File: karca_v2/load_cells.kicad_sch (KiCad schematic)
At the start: 16 parts, among them J4 LoadCell_1_2, J5 LoadCell_3_4, U2 NUP4202, U3 MCP3208, U4 NUP4202, U5 NUP4202, U6 TLV9304xD, U7 TLV9304xD

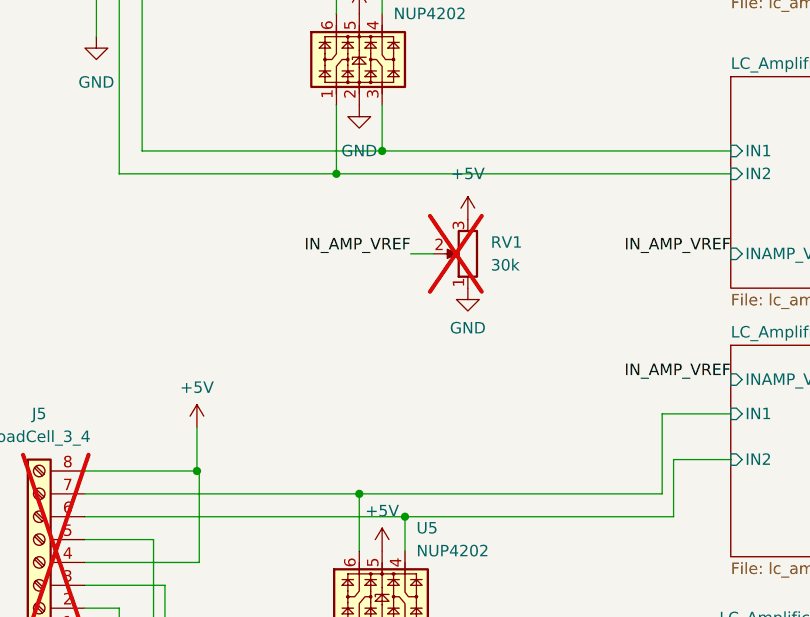
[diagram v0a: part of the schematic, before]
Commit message: reorganized ADCs
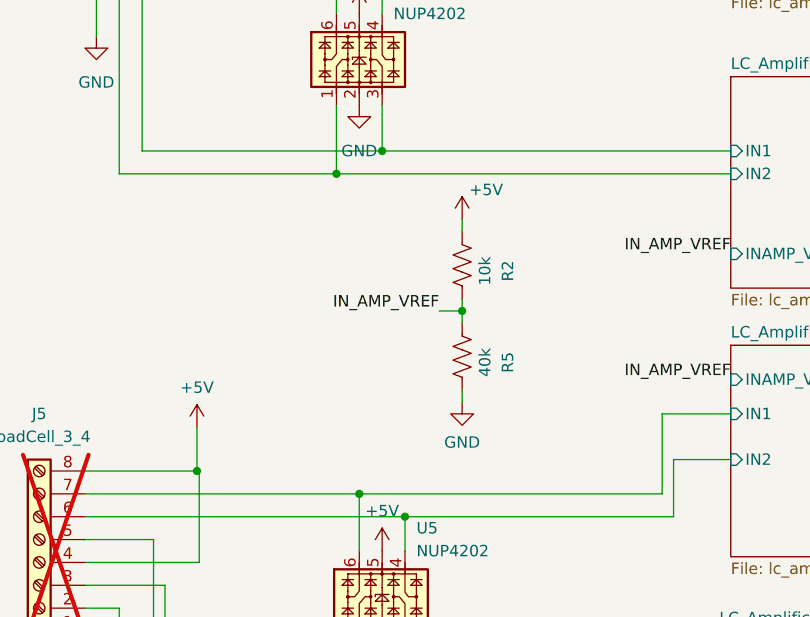
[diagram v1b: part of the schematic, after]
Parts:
- removed RV1: 30k, Potentiometer_THT:Potentiometer_Bourns_3296W_Vertical, symbol Device:R_Potentiometer
- added R2: 10k, Resistor_SMD:R_1206_3216Metric, symbol Device:R_US
- added R5: 40k, Resistor_SMD:R_1206_3216Metric, symbol Device:R_US
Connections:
- net +5V: now also R2.1
- net GND: now also R5.2
- net IN_AMP_VREF: now also R2.2, R5.1
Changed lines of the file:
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@@
 	(title_block
 		(title "kARCA 2.0 Engine Control System")
-		(date "2024-12-16")
-		(rev "1.1")
+		(date "2026-03-23")
+		(rev "1.2")
 		(company "Rice Eclipse")
 		(comment 1 "Designed by Deepak Narayan")
@@
 	)
 	(junction
+		(at 104.14 87.63)
+		(diameter 0)
+		(color 0 0 0 0)
+	)
+	(junction
 		(at 213.995 104.14)
 		(diameter 0)
@@
 	(wire
 		(pts
-			(xy 100.965 81.28) (xy 98.425 81.28)
+			(xy 104.14 87.63) (xy 101.6 87.63)
 		)
 		(stroke
@@
 	(wire
 		(pts
+			(xy 104.14 96.52) (xy 104.14 97.79)
+		)
+		(stroke
+			(width 0)
+			(type default)
+		)
+	)
+	(wire
+		(pts
 			(xy 133.985 104.14) (xy 127.635 104.14)
 		)
@@
 	(wire
 		(pts
+			(xy 104.14 87.63) (xy 104.14 88.9)
+		)
+		(stroke
+			(width 0)
+			(type default)
+		)
+	)
+	(wire
+		(pts
 			(xy 213.995 104.14) (xy 216.281 104.14)
 		)
@@
 	(wire
 		(pts
+			(xy 104.14 86.36) (xy 104.14 87.63)
+		)
+		(stroke
+			(width 0)
+			(type default)
+		)
+	)
+	(wire
+		(pts
 			(xy 95.25 154.94) (xy 95.25 151.13)
 		)
@@
 	(wire
 		(pts
+			(xy 104.14 77.47) (xy 104.14 78.74)
+		)
+		(stroke
+			(width 0)
+			(type default)
+		)
+	)
+	(wire
+		(pts
 			(xy 92.71 124.46) (xy 92.71 132.08)
 		)
@@
 	)
 	(label "IN_AMP_VREF"
-		(at 98.425 81.28 180)
+		(at 101.6 87.63 180)
 		(effects
 			(font
@@
 	)
 	(symbol
-		(lib_id "Device:R_Potentiometer")
-		(at 104.775 81.28 180)
+		(lib_id "Device:R_US")
+		(at 104.14 92.71 0)
 		(unit 1)
 		(exclude_from_sim no)
-		(in_bom no)
+		(in_bom yes)
 		(on_board yes)
-		(dnp yes)
-		(fields_autoplaced yes)
-		(property "Reference" "RV1"
-			(at 107.315 80.01 0)
+		(dnp no)
+		(property "Reference" "R5"
+			(at 109.22 93.345 90)
 			(effects
 				(font
 					(size 1.27 1.27)
 				)
-				(justify right)
 			)
 		)
-		(property "Value" "30k"
-			(at 107.315 82.55 0)
+		(property "Value" "40k"
+			(at 106.68 93.345 90)
 			(effects
 				(font
 					(size 1.27 1.27)
 				)
-				(justify right)
 			)
 		)
-		(property "Footprint" "Potentiometer_THT:Potentiometer_Bourns_3296W_Vertical"
-			(at 104.775 81.28 0)
+		(property "Footprint" "Resistor_SMD:R_1206_3216Metric"
+			(at 105.156 92.964 90)
 			(effects
 				(font
@@
 		)
 		(property "Datasheet" "~"
-			(at 104.775 81.28 0)
+			(at 104.14 92.71 0)
 			(effects
 				(font
@@
 		)
 		(property "Description" ""
-			(at 104.775 81.28 0)
+			(at 104.14 92.71 0)
 			(effects
 				(font
@@
 			)
 		)
-		(pin "3"
+		(pin "1"
+		)
+		(pin "2"
+		)
+		(instances
+			(project "karca_v2"
+				(path "/29cf4797-56f2-4f57-ae95-7df639362e3c/ddbef897-b93d-4056-8606-b8e89931524a"
+					(reference "R5")
+					(unit 1)
+				)
+			)
+		)
+	)
+	(symbol
+		(lib_id "Device:R_US")
+		(at 104.14 82.55 0)
+		(unit 1)
+		(exclude_from_sim no)
+		(in_bom yes)
+		(on_board yes)
+		(dnp no)
+		(property "Reference" "R2"
+			(at 109.22 83.185 90)
+			(effects
+				(font
+					(size 1.27 1.27)
+				)
+			)
+		)
+		(property "Value" "10k"
+			(at 106.68 83.185 90)
+			(effects
+				(font
+					(size 1.27 1.27)
+				)
+			)
+		)
+		(property "Footprint" "Resistor_SMD:R_1206_3216Metric"
+			(at 105.156 82.804 90)
+			(effects
+				(font
+					(size 1.27 1.27)
+				)
+				(hide yes)
+			)
+		)
+		(property "Datasheet" "~"
+			(at 104.14 82.55 0)
+			(effects
+				(font
+					(size 1.27 1.27)
+				)
+				(hide yes)
+			)
+		)
+		(property "Description" ""
+			(at 104.14 82.55 0)
+			(effects
+				(font
+					(size 1.27 1.27)
+				)
+				(hide yes)
+			)
 		)
 		(pin "1"
@@
 			(project "karca_v2"
 				(path "/29cf4797-56f2-4f57-ae95-7df639362e3c/ddbef897-b93d-4056-8606-b8e89931524a"
-					(reference "RV1")
+					(reference "R2")
 					(unit 1)
 				)
@@
 	(symbol
 		(lib_id "power:+5V")
-		(at 104.775 77.47 0)
+		(at 104.14 77.47 0)
 		(unit 1)
 		(exclude_from_sim no)
@@
 		(on_board yes)
 		(dnp no)
-		(fields_autoplaced yes)
 		(property "Reference" "#PWR021"
-			(at 104.775 81.28 0)
+			(at 104.14 81.28 0)
 			(effects
 				(font
@@
 		)
 		(property "Value" "+5V"
-			(at 104.775 72.39 0)
+			(at 106.807 74.168 0)
 			(effects
 				(font
@@
 		)
 		(property "Footprint" ""
-			(at 104.775 77.47 0)
+			(at 104.14 77.47 0)
 			(effects
 				(font
@@
 		)
 		(property "Datasheet" ""
-			(at 104.775 77.47 0)
+			(at 104.14 77.47 0)
 			(effects
 				(font
@@
 		)
 		(property "Description" ""
-			(at 104.775 77.47 0)
+			(at 104.14 77.47 0)
 			(effects
 				(font
@@
 	(symbol
 		(lib_id "power:GND")
-		(at 104.775 85.09 0)
+		(at 104.14 97.79 0)
 		(mirror y)
 		(unit 1)
@@
 		(fields_autoplaced yes)
 		(property "Reference" "#PWR023"
-			(at 104.775 91.44 0)
+			(at 104.14 104.14 0)
 			(effects
 				(font
@@
 		)
 		(property "Value" "GND"
-			(at 104.775 89.535 0)
+			(at 104.14 102.235 0)
 			(effects
 				(font
@@
 		)
 		(property "Footprint" ""
-			(at 104.775 85.09 0)
+			(at 104.14 97.79 0)
 			(effects
 				(font
@@
 		)
 		(property "Datasheet" ""
-			(at 104.775 85.09 0)
+			(at 104.14 97.79 0)
 			(effects
 				(font
@@
 		)
 		(property "Description" ""
-			(at 104.775 85.09 0)
+			(at 104.14 97.79 0)
 			(effects
 				(font

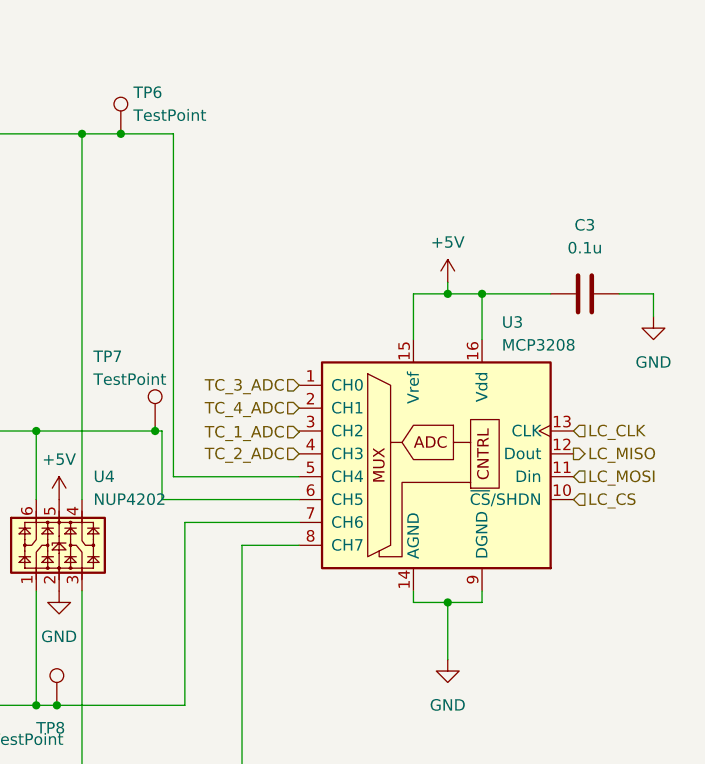
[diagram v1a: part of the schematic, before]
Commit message: finished schematic for v2.1
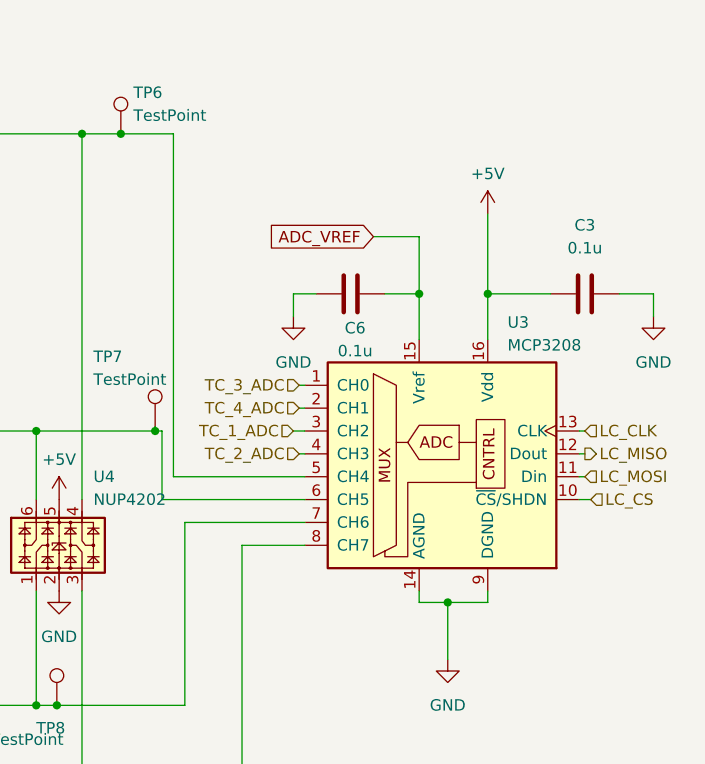
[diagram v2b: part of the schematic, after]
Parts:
- added C6: 0.1u, Capacitor_SMD:C_1206_3216Metric, symbol Device:C
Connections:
- net +5V: no longer U3.15 (Vref)
- net GND: now also C6.1
- new net ADC_VREF: C6.2, U3.15 (Vref)
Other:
- moved on the sheet: U3
